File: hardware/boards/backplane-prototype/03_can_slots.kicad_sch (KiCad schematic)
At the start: 15 parts, among them J1 SLOT_1, J2 XY308-2.54-3P / EXTERNAL CAN, J3 SLOT_2, J4 SLOT_3, J6 SLOT_4, J7 SLOT_5, J8 SLOT_6, U5 TCAN3413DR

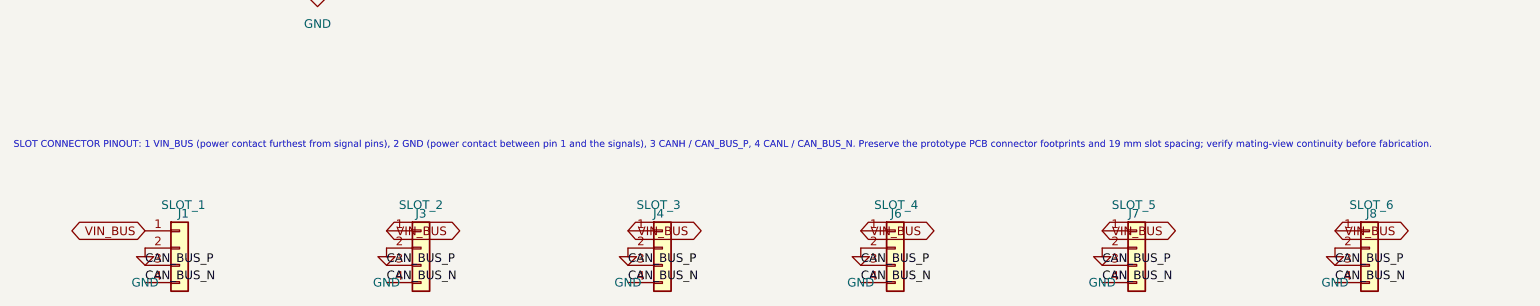
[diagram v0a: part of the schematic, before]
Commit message: use official 12V and VCC power symbols
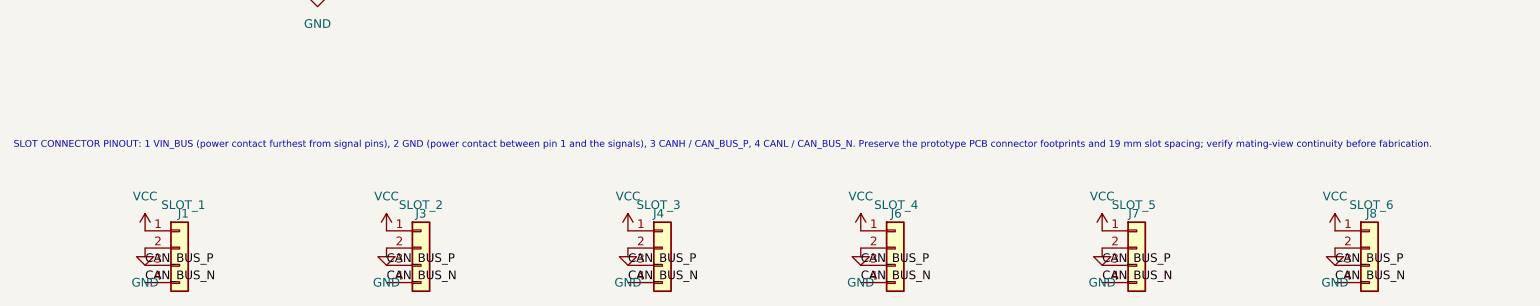
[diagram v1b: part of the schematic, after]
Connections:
- net VIN_BUS renamed VCC
